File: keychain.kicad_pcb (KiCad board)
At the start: 2 copper layers, 41 x 39 mm, 32 parts, among them P1 USB_OTG, P2 VBAT, P3 CONN_01X04, Q1 FDN340P, SW1 BUTTON_SMALL, U1 EFM32HG308

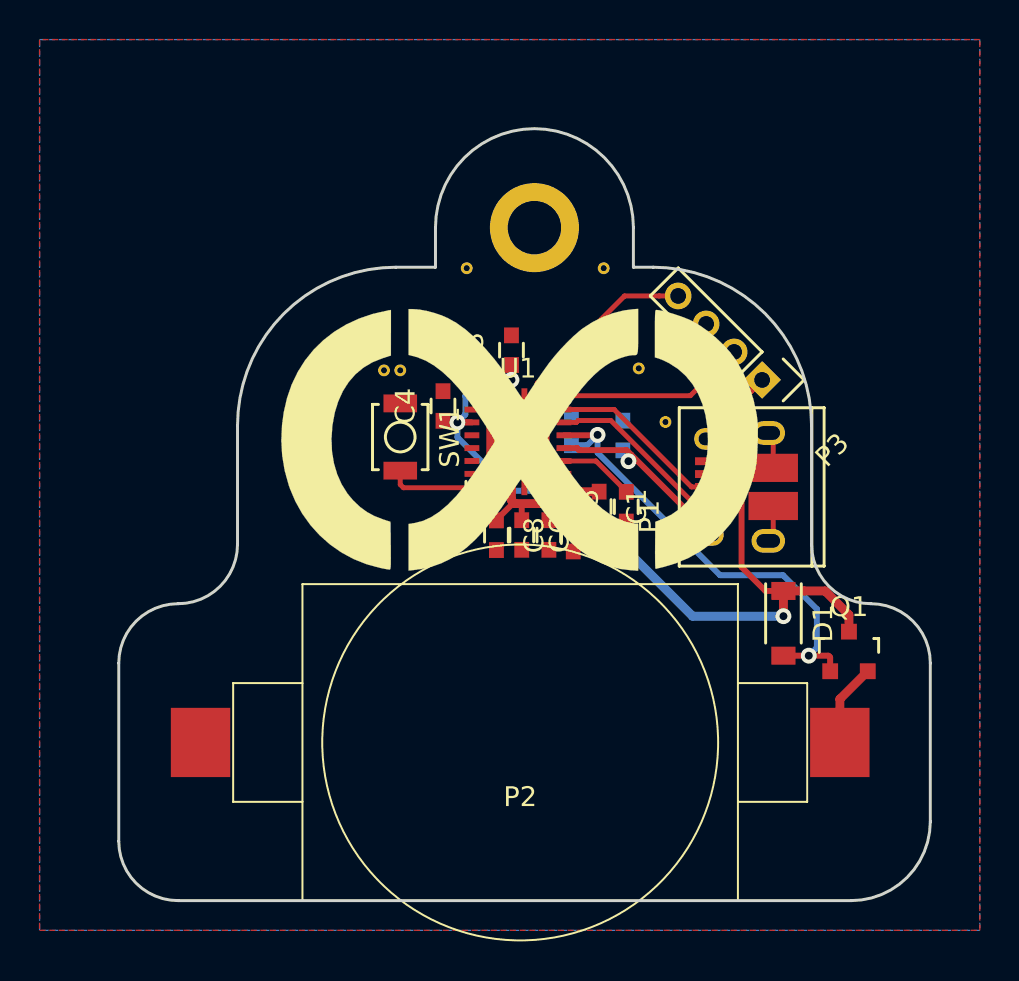
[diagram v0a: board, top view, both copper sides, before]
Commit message: Switched to EFM32TG110, redid board layout
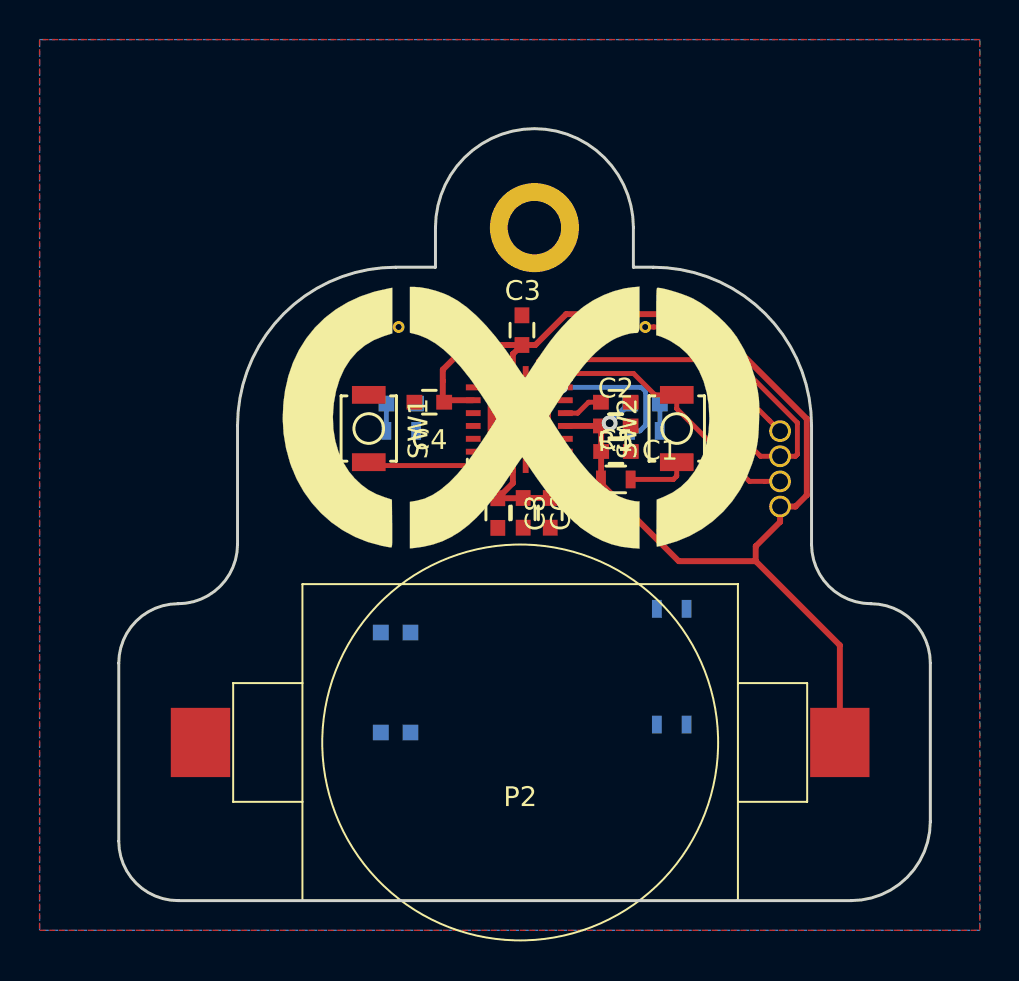
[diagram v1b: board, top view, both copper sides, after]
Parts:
- removed C10: 4.7uF, Capacitors_SMD:C_0603
- removed C9: 1uF, Capacitors_SMD:C_0603
- removed P1: USB_OTG, Connect:USB_Micro-B_10103594-0001LF
- removed Q1: FDN340P, TO_SOT_Packages_SMD:SOT-23
- removed the REF** at (156.6, 91.8)
- removed the REF** at (153.5, 84.1)
- removed the REF** at (146.6, 84.0)
- removed the REF** at (142.4, 89.2)
- removed the REF** at (149.0, 93.6)
- removed the REF** at (148.4, 92.9)
- added D2: Blue, LEDs:LED_0603, B.Cu at (155.6, 90.9)
- added D3: LED_Small, LEDs:LED_0603, B.Cu at (143.0, 107.5)
- added D4: LED_Small, LEDs:LED_0603, B.Cu at (143.0, 102.5)
- added R1: 4.7K, Resistors_SMD:R_0603, F.Cu at (154.1, 94.7)
- added R2: R_Small, Resistors_SMD:R_0603, B.Cu at (143.3, 92.3)
- added R3: R_Small, Resistors_SMD:R_0603, B.Cu at (155.6, 92.3)
- added R4: R_Small, Resistors_SMD:R_0603, B.Cu at (156.9, 107.1)
- added R5: R_Small, Resistors_SMD:R_0603, B.Cu at (156.9, 101.3)
- added REF**: VIA_0.6mm, GNDVIA:GND_VIA_0.6mm, F.Cu at (149.3, 91.6)
- added REF**: VIA_0.6mm, GNDVIA:GND_VIA_0.6mm, F.Cu at (158.2, 95.9)
- added REF**: VIA_0.6mm, GNDVIA:GND_VIA_0.6mm, F.Cu at (159.9, 91.5)
- added SW2: BOOT, Buttons_Switches_SMD:SW_SPST_B3U-1000P, F.Cu at (157.2, 92.2)
- D1: value 1N4148W -> Blue; footprint Diodes_SMD:SOD-123 -> LEDs:LED_0603; moved to B.Cu
- P3: footprint Pin_Headers:Pin_Header_Straight_1x04_Pitch2.00mm -> Pin_header_extra:CONN_01X04_1.27mm
- SW1: value BUTTON_SMALL -> ~RESET~
- U1: value EFM32HG308 -> EFM32TG110
- moved D1 22.3 mm to (143.3, 90.9), turned to 0 degrees
- moved C2 5.99 mm to (154.1, 92.0), turned to 0 degrees
- moved C5 5.31 mm to (154.1, 90.8), turned to 180 degrees
- moved P3 3.96 mm to (162.4, 93.5), turned to 180 degrees
- moved C1 2.91 mm to (154.1, 93.3), turned to 0 degrees
- moved REF** 2.26 mm to (143.1, 87.0)
- moved REF** 2.12 mm to (155.6, 87.0)
- moved SW1 1.65 mm to (141.6, 92.2)
- moved REF** 1.42 mm to (148.6, 92.6)
- moved REF** 1.40 mm to (148.7, 90.5)
- moved REF** 1.38 mm to (150.1, 90.5)
- moved C3 1.14 mm to (149.4, 87.2)
- moved C7 1.12 mm to (150.8, 96.4)
- moved U1 1.12 mm to (149.2, 91.7)
- moved C6 1.12 mm to (149.4, 96.4)
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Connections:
- net /SWCLK renamed SWCLK
- net /SWDIO renamed SWDIO
- net Net-(SW1-Pad2) renamed /~RST~
- D1 pad 1: +3V3 -> Net-(D1-Pad1)
- D1 pad 2: /VREGO -> +3V3
- P2 pad 2: /VBAT -> +3V3
- U1 pad 13: +3V3 -> Net-(U1-Pad13)
- U1 pad 14: Net-(C5-Pad2) -> Net-(U1-Pad14)
- U1 pad 15: /VBUS -> +3V3
- U1 pad 16: /VREGO -> Net-(C5-Pad2)
- U1 pad 17: /USB_D- -> Net-(U1-Pad17)
- U1 pad 18: /USB_D+ -> LED2
- U1 pad 3: Net-(U1-Pad3) -> LED1
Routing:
- net /VREGO: track 24.3 -> 0.00 mm, vias 2 -> 0
- net +3V3: track 58.8 -> 71.6 mm, vias 4 -> 1
- net GND: track 5.39 -> 15.8 mm
- net /VBUS: track 9.85 -> 0.00 mm, vias 1 -> 0
- net /USB_D-: track 9.15 -> 0.00 mm
- net /USB_D+: track 9.07 -> 0.00 mm
- net LED2: track 0.00 -> 6.92 mm, vias 0 -> 1
- net SWDIO: track 9.57 -> 14.4 mm
- net /VBAT: track 4.18 -> 0.00 mm
- net SWCLK: track 10.2 -> 14.2 mm
- net Net-(R1-Pad2): track 0.00 -> 3.37 mm
- net Net-(C5-Pad2): track 3.81 -> 2.03 mm
- net Net-(D2-Pad1): track 0.00 -> 1.38 mm
- net Net-(D1-Pad1): track 0.00 -> 1.38 mm
- net /~RST~: track 5.09 -> 6.05 mm

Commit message: More or less done.
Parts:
- removed C4: 100nF, Capacitors_SMD:C_0603
- removed the REF** at (143.1, 87.0)
- removed the REF** at (155.6, 87.0)
- added L1: BLM21B102S, Capacitors_SMD:C_0805, F.Cu at (154.4, 97.1)
- added P1: CAP_SLIDER, capsense:slider_2p, B.Cu at (149.4, 107.5)
- added R6: 1R, Resistors_SMD:R_0603, F.Cu at (152.0, 96.3)
- added R7: 100R, Resistors_SMD:R_0603, F.Cu at (154.1, 89.8)
- added R8: 100R, Resistors_SMD:R_0603, F.Cu at (144.6, 92.0)
- added REF**: VIA_0.6mm, GNDVIA:GND_VIA_0.6mm, F.Cu at (168.1, 107.8)
- added REF**: VIA_0.6mm, GNDVIA:GND_VIA_0.6mm, F.Cu at (130.8, 108.0)
- added REF**: VIA_0.6mm, GNDVIA:GND_VIA_0.6mm, F.Cu at (159.4, 98.4)
- added REF**: VIA_0.6mm, GNDVIA:GND_VIA_0.6mm, F.Cu at (149.1, 115.0)
- C7, C8: value 100nF -> 10nF
- R2, R3, R4, R5: moved to F.Cu
- moved D3 16.4 mm to (155.6, 97.0), turned to 90 degrees
- moved R5 14.4 mm to (143.2, 97.0), turned to 90 degrees
- moved C2 9.59 mm to (144.6, 90.6), turned to 180 degrees
- moved R4 8.93 mm to (158.9, 98.4)
- moved R2 6.14 mm to (142.9, 86.1), turned to 270 degrees
- moved R3 6.10 mm to (155.7, 86.2), turned to 270 degrees
- moved D4 5.49 mm to (143.1, 97.0), turned to 90 degrees
- moved D1 4.76 mm to (143.1, 86.1), turned to 270 degrees
- moved D2 4.76 mm to (155.6, 86.1), turned to 270 degrees
- moved C5 0.33 mm to (154.1, 91.2)
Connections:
- C6 pad 1: +3V3 -> VDDA
- C7 pad 1: +3V3 -> VDDA
- C8 pad 1: +3V3 -> VDDA
- D1 pad 2: +3V3 -> LED1
- D2 pad 2: +3V3 -> LED2
- D3 pad 2: +3V3 -> LED3
- D4 pad 2: +3V3 -> LED4
- R2 pad 1: LED1 -> Net-(D1-Pad1)
- R2 pad 2: Net-(D1-Pad1) -> GND
- R3 pad 1: LED2 -> Net-(D2-Pad1)
- R3 pad 2: Net-(D2-Pad1) -> GND
- R4 pad 1: LED3 -> Net-(D3-Pad1)
- R4 pad 2: Net-(D3-Pad1) -> GND
- R5 pad 1: LED4 -> Net-(D4-Pad1)
- R5 pad 2: Net-(D4-Pad1) -> GND
- U1 pad 1: Net-(U1-Pad1) -> (no net)
- U1 pad 10: Net-(U1-Pad10) -> (no net)
- U1 pad 11: Net-(U1-Pad11) -> (no net)
- U1 pad 12: +3V3 -> VDDA
- U1 pad 13: Net-(U1-Pad13) -> LED3
- U1 pad 14: Net-(U1-Pad14) -> (no net)
- U1 pad 17: Net-(U1-Pad17) -> CAP_S_2
- U1 pad 18: LED2 -> (no net)
- U1 pad 21: Net-(U1-Pad21) -> LED2
- U1 pad 23: Net-(U1-Pad23) -> (no net)
- U1 pad 24: Net-(U1-Pad24) -> LED1
- U1 pad 3: LED1 -> (no net)
- U1 pad 4: Net-(U1-Pad4) -> CAP_S_1
- U1 pad 5: Net-(U1-Pad5) -> (no net)
- U1 pad 6: Net-(U1-Pad6) -> (no net)
- U1 pad 8: Net-(U1-Pad8) -> LED4
- U1 pad 9: +3V3 -> VDDA
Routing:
- net Net-(P1-Pad2): track 0.00 -> 21.3 mm, vias 0 -> 1
- net Net-(P1-Pad1): track 0.00 -> 19.1 mm, vias 0 -> 1
- net +3V3: track 71.6 -> 57.8 mm, vias 1 -> 0
- net GND: track 15.8 -> 4.58 mm
- net VDDA: track 0.00 -> 7.43 mm
- net LED4: track 0.00 -> 6.57 mm, vias 0 -> 1
- net LED1: track 0.00 -> 5.94 mm, vias 0 -> 1
- net LED3: track 0.00 -> 5.71 mm, vias 0 -> 1
- net Net-(D3-Pad1): track 0.00 -> 2.78 mm, vias 0 -> 1
- net CAP_S_2: track 0.00 -> 2.13 mm
- net CAP_S_1: track 0.00 -> 1.57 mm
- net Net-(L1-Pad2): track 0.00 -> 1.41 mm
- net Net-(D2-Pad1): track 1.38 -> 0.13 mm, vias 0 -> 1
- net Net-(D1-Pad1): track 1.38 -> 0.29 mm, vias 0 -> 1
- net Net-(D4-Pad1): track 0.00 -> 0.24 mm, vias 0 -> 1
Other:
- board text added: "BOOT"
- board text added: "RST"

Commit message: Moar changes
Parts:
- added P4: CONN_01X05, Pin_header_extra:CONN_01X05_SMDISH, F.Cu at (136.7, 94.8)
- added REF**: VIA_0.6mm, GNDVIA:GND_VIA_0.6mm, F.Cu at (157.6, 86.8)
- added REF**: VIA_0.6mm, GNDVIA:GND_VIA_0.6mm, F.Cu at (154.9, 92.2)
- added REF**: VIA_0.6mm, GNDVIA:GND_VIA_0.6mm, F.Cu at (153.4, 81.9)
- added REF**: VIA_0.6mm, GNDVIA:GND_VIA_0.6mm, F.Cu at (146.3, 81.9)
- added REF**: VIA_0.6mm, GNDVIA:GND_VIA_0.6mm, F.Cu at (140.8, 86.9)
- added SW3: USR1, smallbutton:SmallButton, B.Cu at (143.5, 91.5)
- added SW4: USR2, smallbutton:SmallButton, B.Cu at (155.4, 91.5)
- R8: moved to B.Cu
- SW1, SW2: footprint Buttons_Switches_SMD:SW_SPST_B3U-1000P -> smallbutton:Tactile_Push_Button_SMD_3x3x1.5mm.kicad_mod
- moved R8 2.64 mm to (143.4, 94.4)
- moved SW1 1.47 mm to (142.6, 93.2), turned to 0 degrees
- moved SW2 0.82 mm to (157.4, 92.9)
- moved REF** 0.50 mm to (149.5, 82.0)
- moved REF** 0.50 mm to (158.9, 98.4)
- moved R2 0.26 mm to (143.2, 86.1)
- moved REF** 0.13 mm to (149.1, 91.6)
- moved R5 0.06 mm to (143.2, 97.0)
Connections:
- U1 pad 1: (no net) -> Net-(SW3-Pad2)
- U1 pad 13: LED3 -> Net-(SW4-Pad1)
- U1 pad 14: (no net) -> LED3
- U1 pad 18: (no net) -> CAP_S_1
- U1 pad 23: (no net) -> LED1
- U1 pad 24: LED1 -> (no net)
- U1 pad 3: (no net) -> Net-(P4-Pad5)
- U1 pad 4: CAP_S_1 -> Net-(P4-Pad4)
- U1 pad 5: (no net) -> Net-(P4-Pad3)
- U1 pad 6: (no net) -> Net-(P4-Pad2)
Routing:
- net Net-(P4-Pad2): track 0.00 -> 11.4 mm
- net Net-(P4-Pad3): track 0.00 -> 11.1 mm
- net Net-(P4-Pad5): track 0.00 -> 11.0 mm
- net Net-(P4-Pad4): track 0.00 -> 10.8 mm
- net CAP_S_1: track 1.57 -> 11.5 mm, vias 0 -> 1
- net /~RST~: track 6.49 -> 0.00 mm
- net Net-(SW4-Pad1): track 0.00 -> 3.29 mm, vias 0 -> 1
- net Net-(P1-Pad1): track 19.1 -> 16.9 mm, vias 1 -> 0
- net Net-(SW3-Pad2): track 0.00 -> 1.55 mm, vias 0 -> 1
- net SWCLK: track 14.6 -> 15.8 mm
- net Net-(R1-Pad2): track 3.37 -> 4.42 mm
- net GND: track 4.58 -> 3.65 mm
- net LED3: track 5.71 -> 6.58 mm
- net LED1: track 5.94 -> 6.64 mm
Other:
- outline, holes or cut-outs redrawn
- net class Default: clearance 0.2 -> 0.1
- net class Power: clearance 0.2 -> 0.1
- rule pad_to_mask_clearance: 0.2 -> 0.15
- rule trace_clearance: 0.2 -> 0.1
